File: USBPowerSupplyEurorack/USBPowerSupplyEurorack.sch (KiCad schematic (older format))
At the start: 19 parts, among them J1 1734366-1, J2 95278-501A10LF, Q1 Q_PMOS_GSD

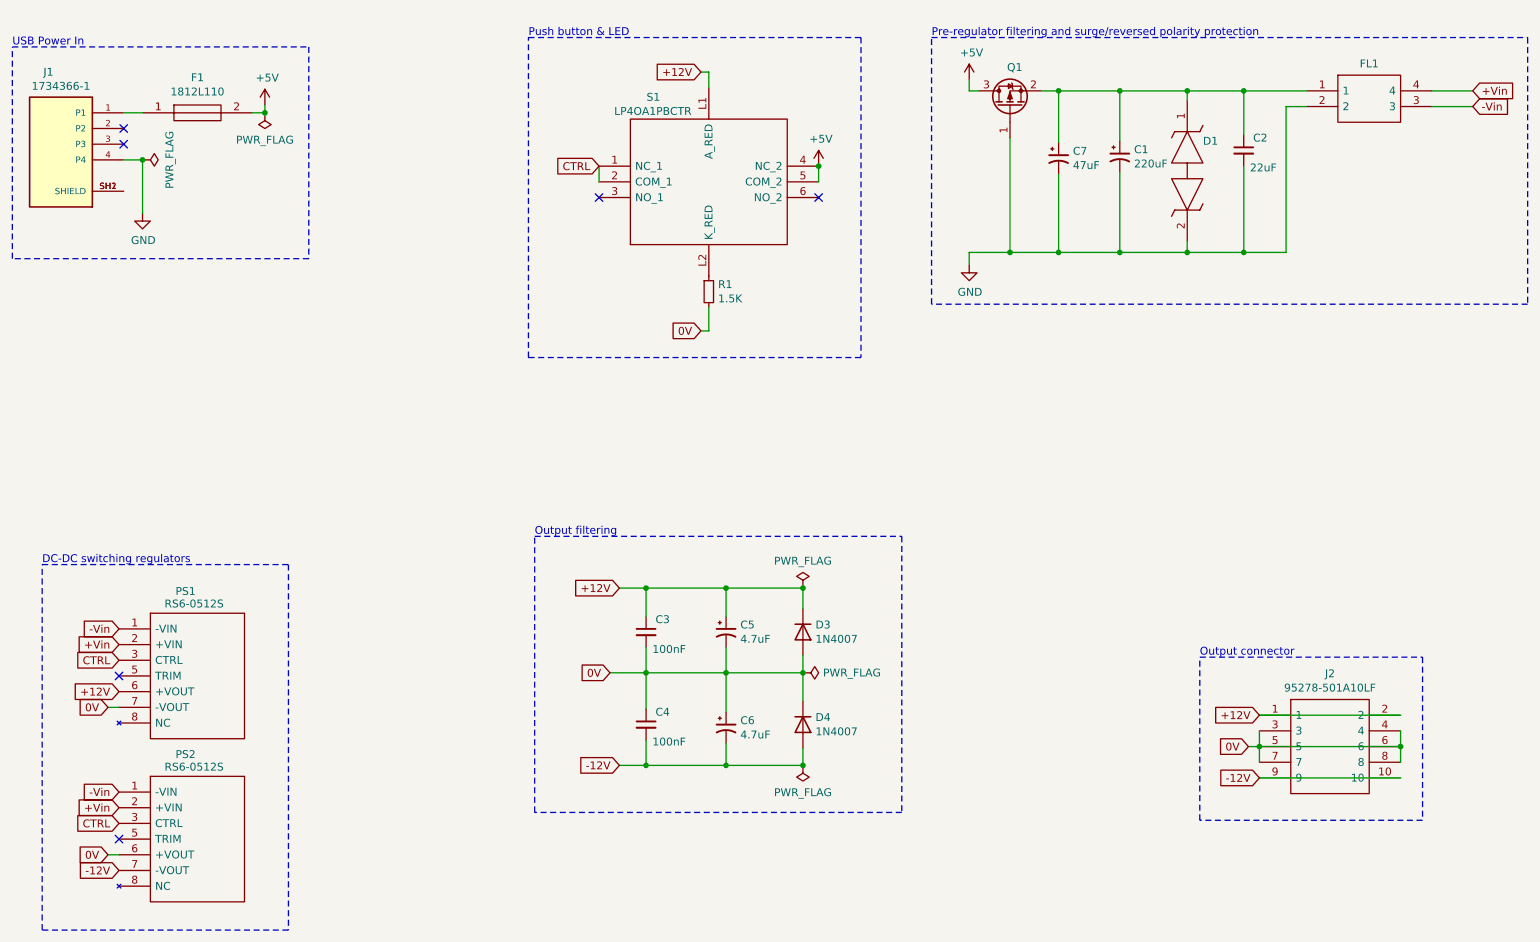
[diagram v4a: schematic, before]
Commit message: simplified schematics
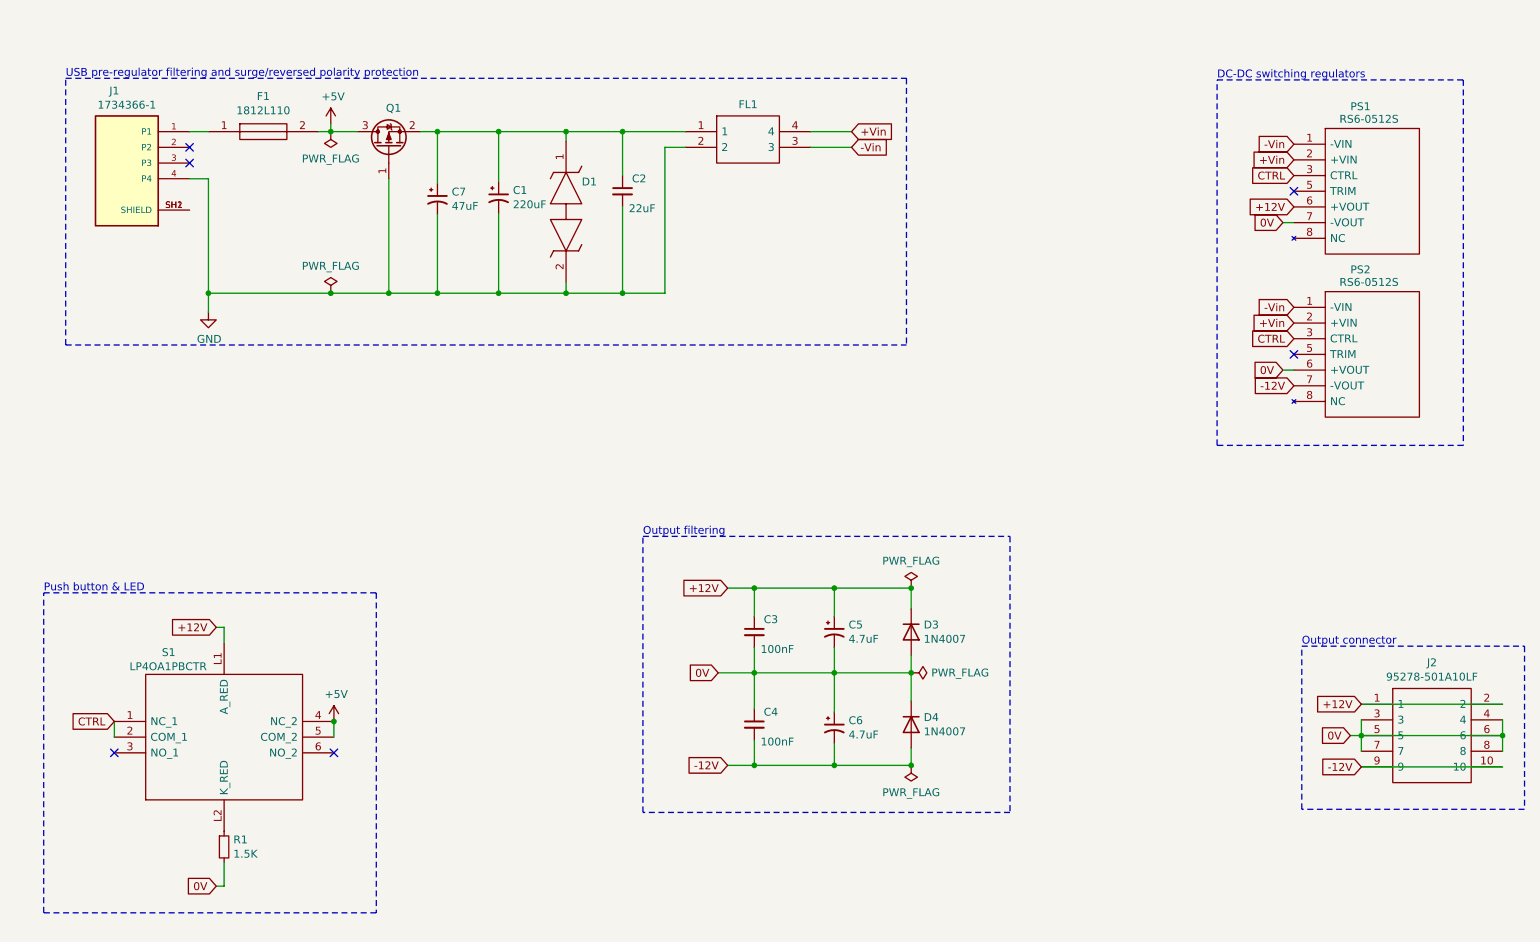
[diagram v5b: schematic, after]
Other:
- note added: "USB pre-regulator filtering and surge/reversed polarity protection"
- note removed: "Pre-regulator filtering and surge/reversed polarity protection"
- note removed: "USB Power In"
- moved on the sheet: C1, C2, C3, C4, C5, C6, C7, D1, D3, D4, F1, FL1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

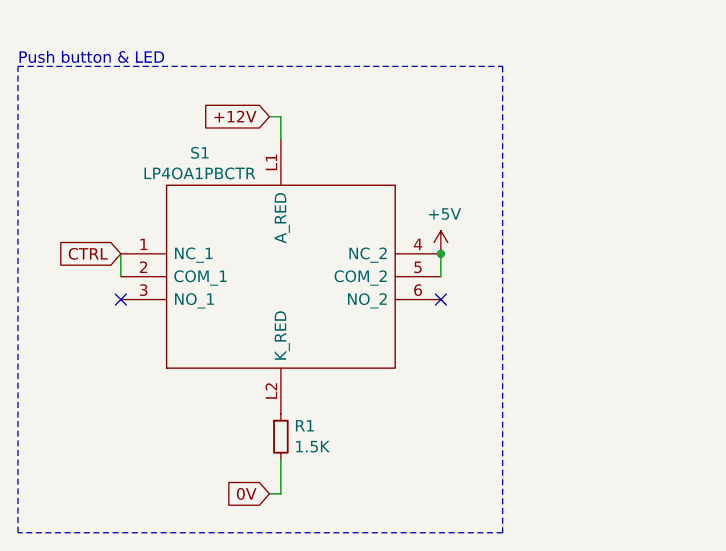
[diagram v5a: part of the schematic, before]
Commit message: added 3D models
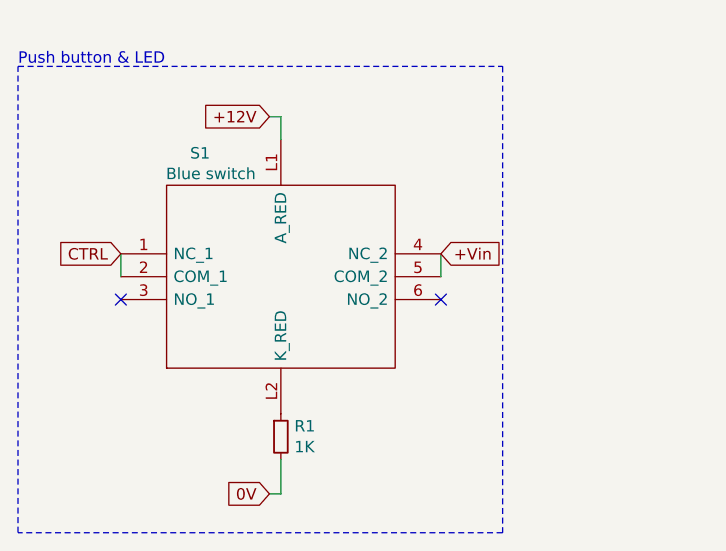
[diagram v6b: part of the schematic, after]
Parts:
- R1: value 1.5K -> 1K; LCSC C4310 -> C17513
- S1: value LP4OA1PBCTR -> Blue switch
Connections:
- net +5V: no longer S1.4 (NC_2), S1.5 (COM_2)
- net +Vin: now also S1.4 (NC_2), S1.5 (COM_2)

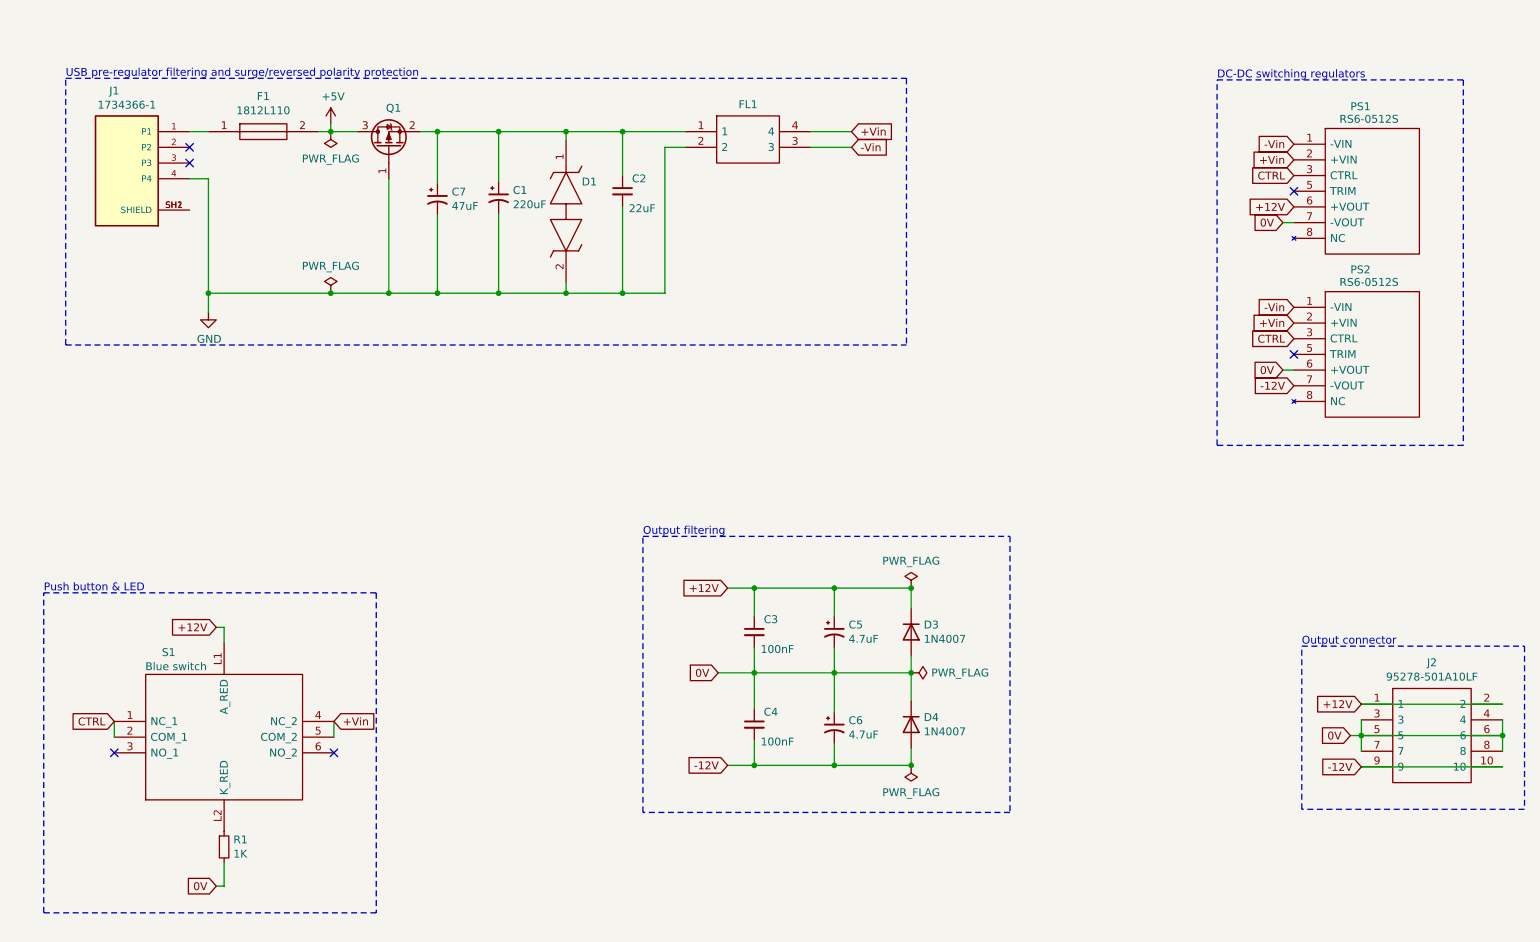
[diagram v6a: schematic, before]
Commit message: removed switch and simplified schematics, added a second LED for -12v
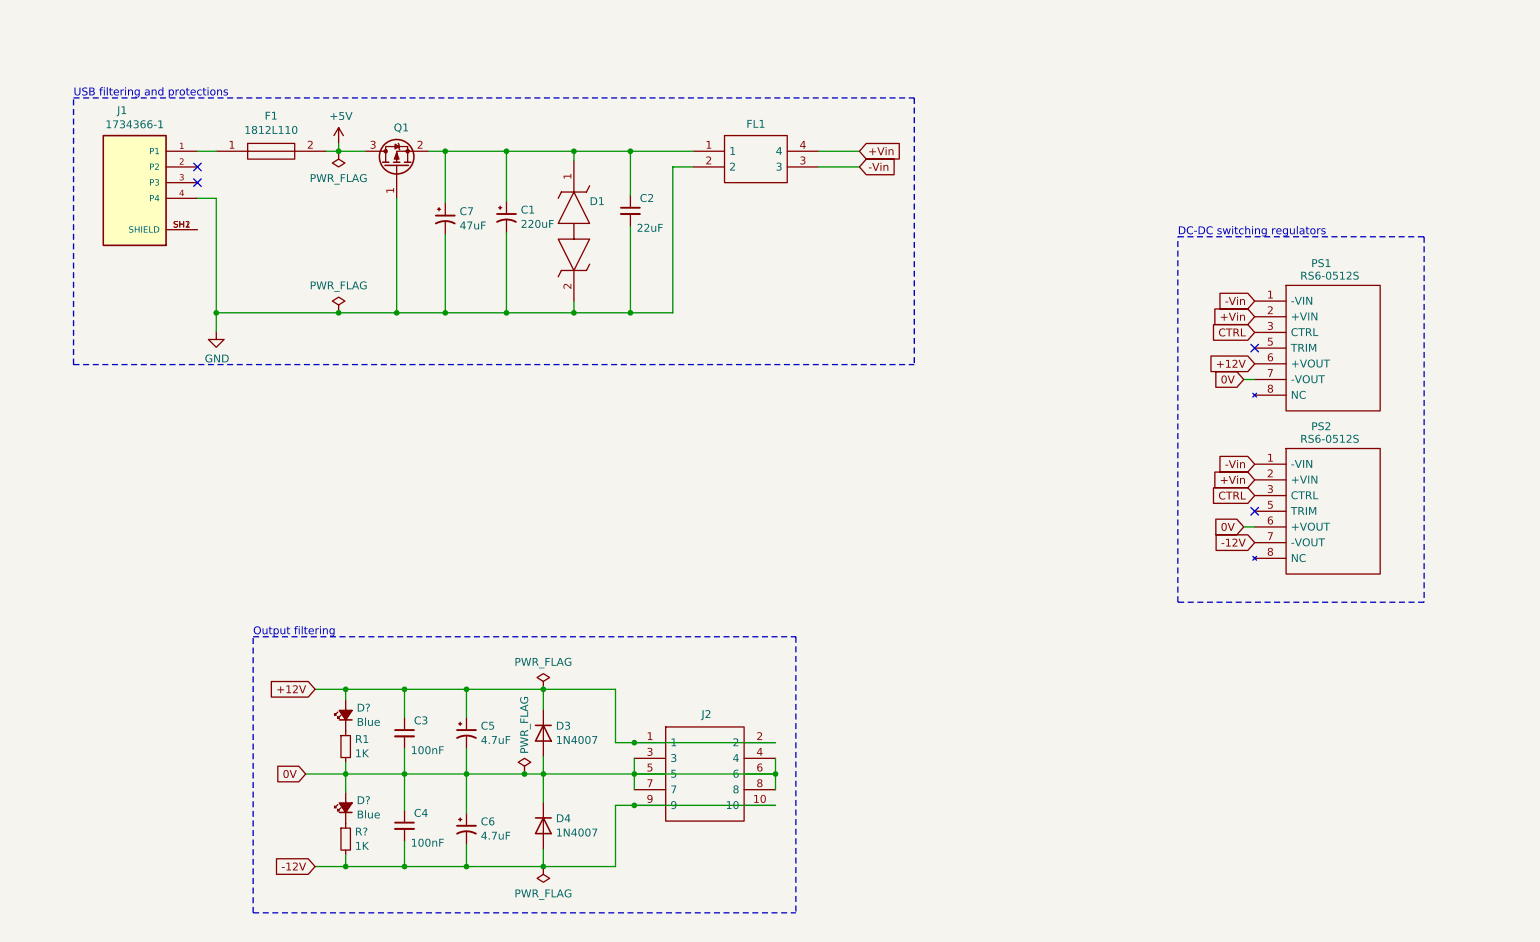
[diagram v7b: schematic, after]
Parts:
- removed S1: Blue switch, LP4OA1PBCTR:LP4OA1PBCTR, symbol LP4OA1PBCTR:LP4OA1PBCTR
- added D? (x2): Blue, symbol Device:LED_Small_ALT
- added R?: 1K, Resistor_SMD:R_0805_2012Metric, symbol Device:R_Small
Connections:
- net +12V: now also D?.2 (A)
- net -12V: now also R?.2
- net 0V: now also D?.2 (A)
- net at R1.1: now also D?.1 (K)
- new net: D?.1 (K), R?.1
- no-connect marks 6 -> 4
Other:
- note added: "USB filtering and protections"
- note removed: "Output connector"
- note removed: "Push button & LED"
- note removed: "USB pre-regulator filtering and surge/reversed polarity protection"
- moved on the sheet: C1, C2, C3, C4, C5, C6, C7, D1, D3, D4, F1, FL1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

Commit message: changed footprints placement, added the two LEDs
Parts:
- gave numbers to parts that had none: 3
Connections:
- net GND: now also J1.SH1 (SHIELD), J1.SH2 (SHIELD)
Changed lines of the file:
@@
 	2250 2765 3030 2765
 Wire Wire Line
-	2250 2035 2250 2765
+	2250 2035 2250 2235
 Wire Wire Line
 	5160 1835 5160 2765
@@
 Connection ~ 4915 5905
 $Comp
-L Device:LED_Small_ALT D?
+L Device:LED_Small_ALT D2
 U 1 1 5FF1E6C4
 P 3075 5330
-F 0 "D?" V 3121 5260 50  0000 R CNN
+F 0 "D2" V 3121 5260 50  0000 R CNN
 F 1 "Blue" V 3030 5260 50  0000 R CNN
 F 2 "" V 3075 5330 50  0001 C CNN
@@
 	3075 5165 3450 5165
 $Comp
-L Device:R_Small R?
+L Device:R_Small R2
 U 1 1 5FF3D1E7
 P 3075 6120
-F 0 "R?" H 3134 6166 50  0000 L CNN
+F 0 "R2" H 3134 6166 50  0000 L CNN
 F 1 "1K" H 3134 6075 50  0000 L CNN
 F 2 "Resistor_SMD:R_0805_2012Metric" H 3075 6120 50  0001 C CNN
@@
 $EndComp
 $Comp
-L Device:LED_Small_ALT D?
+L Device:LED_Small_ALT D5
 U 1 1 5FF3D1ED
 P 3075 5920
-F 0 "D?" V 3121 5850 50  0000 R CNN
+F 0 "D5" V 3121 5850 50  0000 R CNN
 F 1 "Blue" V 3030 5850 50  0000 R CNN
 F 2 "" V 3075 5920 50  0001 C CNN
@@
 Wire Wire Line
 	3075 6295 2880 6295
+Wire Wire Line
+	2130 2235 2250 2235
+Connection ~ 2250 2235
+Wire Wire Line
+	2250 2235 2250 2765
 $EndSCHEMATC
